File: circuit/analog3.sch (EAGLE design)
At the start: 74 parts, among them IC1 AD8603UJ, IC2 74HC4052D, IC3 AD8603UJ, IC4 AD8221R, IC5 AD8221R, IC6 LM258, IC7 LM258

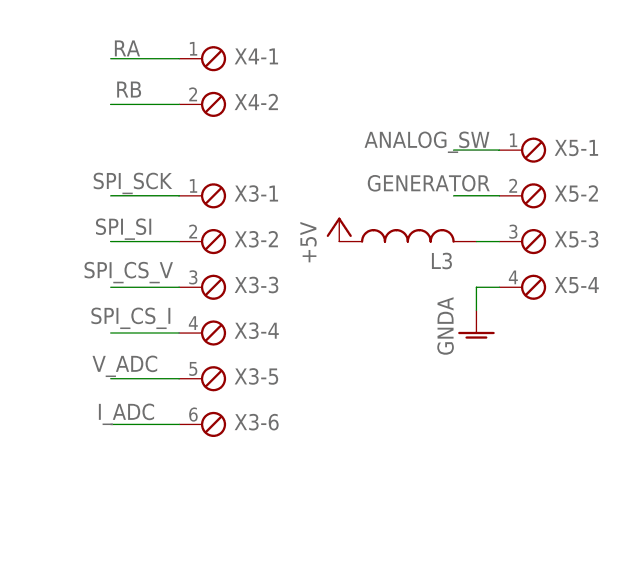
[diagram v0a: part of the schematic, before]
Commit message: - поменяли местами питание и землю
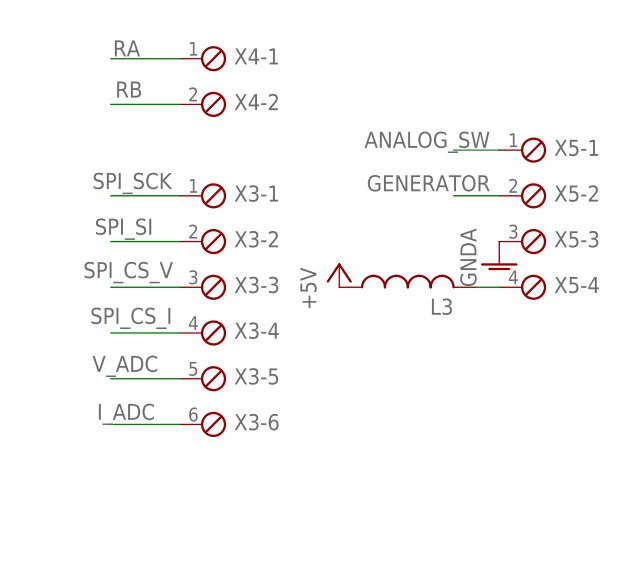
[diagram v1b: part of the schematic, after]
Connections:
- net GNDA: now also X5-3.1; no longer X5-4.1
- net N$6: now also X5-4.1; no longer X5-3.1
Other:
- moved on the sheet: L3
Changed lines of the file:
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@@
 <instance part="X4" gate="-1" x="149.86" y="93.98"/>
 <instance part="X4" gate="-2" x="149.86" y="88.9"/>
-<instance part="P+7" gate="1" x="165.1" y="76.2"/>
+<instance part="P+7" gate="1" x="165.1" y="71.12"/>
 <instance part="GND1" gate="1" x="15.24" y="63.5"/>
 <instance part="GND2" gate="1" x="-22.86" y="63.5"/>
@@
 <instance part="GND23" gate="1" x="-7.62" y="10.16"/>
 <instance part="IC1" gate="G$1" x="-40.64" y="76.2" rot="MR0"/>
-<instance part="L3" gate="G$1" x="172.72" y="73.66" rot="R90"/>
+<instance part="L3" gate="G$1" x="172.72" y="68.58" rot="R90"/>
 <instance part="C3" gate="G$1" x="48.26" y="86.36"/>
 <instance part="P+2" gate="1" x="93.98" y="40.64"/>
@@
 <instance part="X5" gate="-3" x="185.42" y="73.66"/>
 <instance part="X5" gate="-4" x="185.42" y="68.58"/>
-<instance part="GND26" gate="1" x="180.34" y="63.5"/>
+<instance part="GND26" gate="1" x="182.88" y="71.12"/>
 </instances>
 <busses>
@@
 </segment>
 <segment>
+<pinref part="X5" gate="-3" pin="1"/>
 <pinref part="GND26" gate="1" pin="GNDA"/>
-<wire x1="180.34" y1="66.04" x2="180.34" y2="68.58" width="0.1524" layer="91"/>
-<pinref part="X5" gate="-4" pin="1"/>
-<wire x1="180.34" y1="68.58" x2="182.88" y2="68.58" width="0.1524" layer="91"/>
 </segment>
 </net>
@@
 <net name="N$6" class="0">
 <segment>
+<pinref part="X5" gate="-4" pin="1"/>
 <pinref part="L3" gate="G$1" pin="2"/>
-<pinref part="X5" gate="-3" pin="1"/>
-<wire x1="180.34" y1="73.66" x2="182.88" y2="73.66" width="0.1524" layer="91"/>
-</segment>
-</net>
+<wire x1="182.88" y1="68.58" x2="180.34" y2="68.58" width="0.1524" layer="91"/>
+</segment>
+</net>

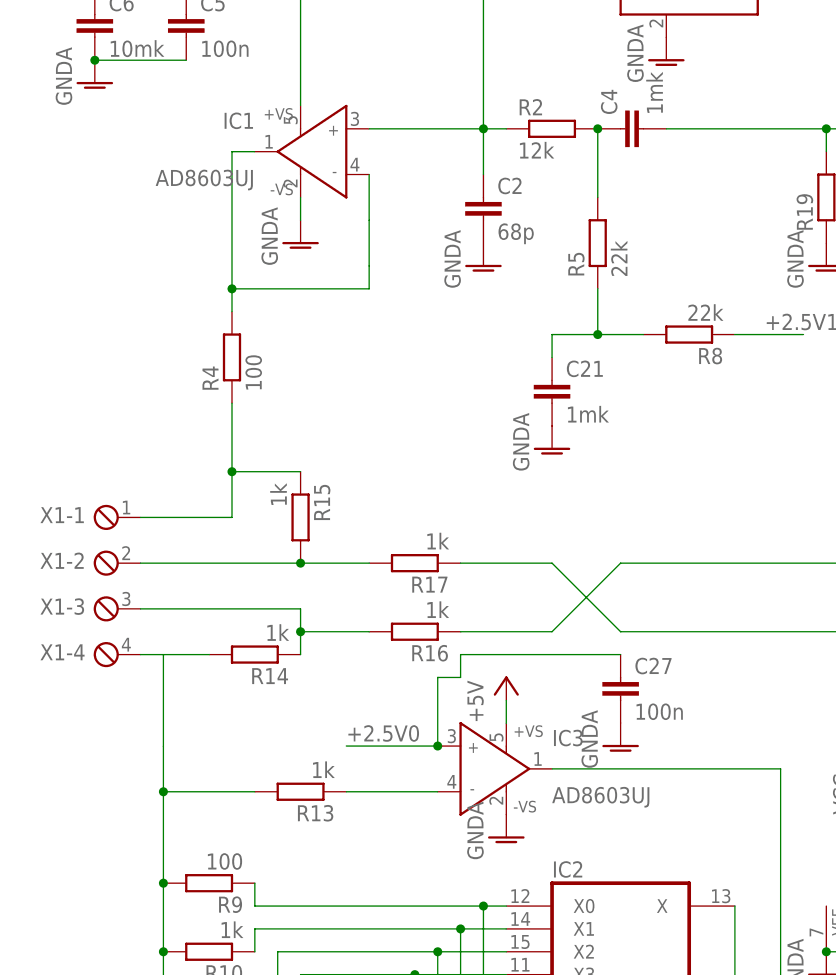
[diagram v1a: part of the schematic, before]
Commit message: - допаяли схему. - PC6 USB_ON подключили - PB10 AN_SW подключили
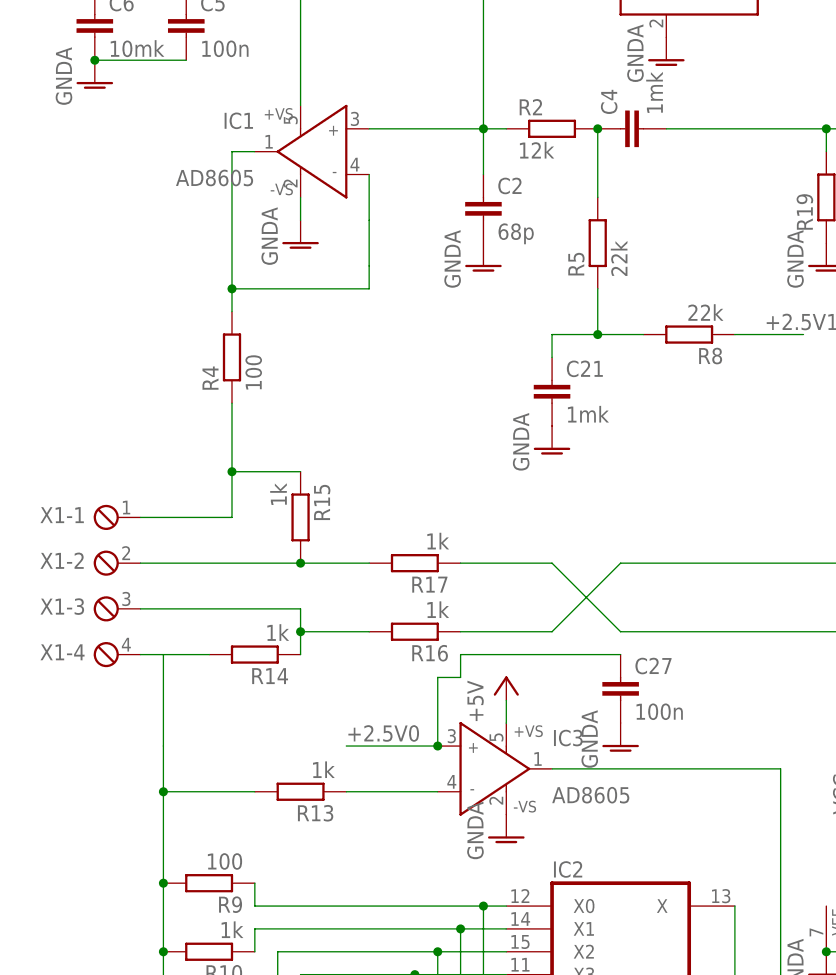
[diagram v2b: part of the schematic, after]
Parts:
- IC1, IC3: value AD8603UJ -> AD8605
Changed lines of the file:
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@@
 <part name="R29" library="rcl" deviceset="R-EU_" device="R0805" value="5"/>
 <part name="GND7" library="supply1" deviceset="GNDA" device=""/>
-<part name="IC3" library="analog-devices" deviceset="AD8603" device="UJ"/>
+<part name="IC3" library="analog-devices" deviceset="AD8603" device="UJ" value="AD8605"/>
 <part name="R19" library="rcl" deviceset="R-EU_" device="R0603" value="3k"/>
 <part name="R22" library="rcl" deviceset="R-EU_" device="R0603" value="12k"/>
@@
 <part name="C27" library="rcl" deviceset="C-EU" device="C0603" value="100n"/>
 <part name="GND23" library="supply1" deviceset="GNDA" device=""/>
-<part name="IC1" library="analog-devices" deviceset="AD8603" device="UJ"/>
+<part name="IC1" library="analog-devices" deviceset="AD8603" device="UJ" value="AD8605"/>
 <part name="L3" library="rcl" deviceset="L-US" device="0204/7"/>
 <part name="C3" library="rcl" deviceset="C-EU" device="C0805" value="10mk"/>
